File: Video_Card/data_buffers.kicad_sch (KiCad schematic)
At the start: 2 parts, among them U1 74FCT16245

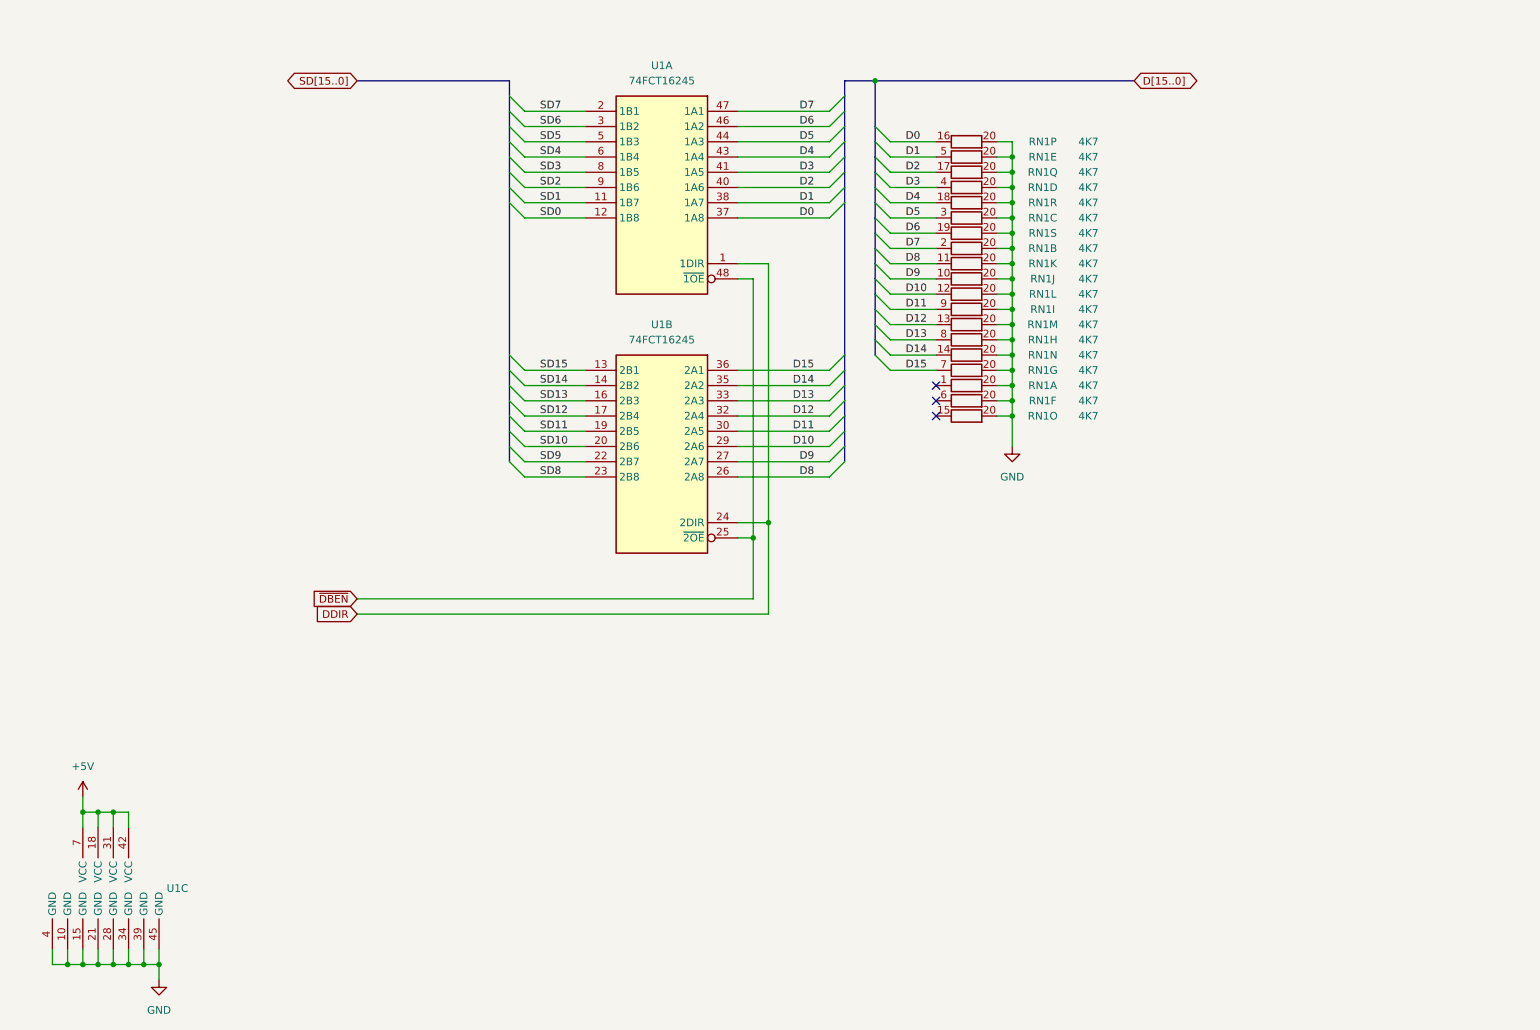
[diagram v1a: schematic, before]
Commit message: Work to date
So much to list ....

* Changed expansion ROM to 16 bit wide to remove some components
* Tried moving peripherals over to an 8 bit dedicated bus, but will have to revert this to reduce component count
* Fleshed out keyboard and I2C controller circuits
* Tried to fit in a font RAM, but I am 50/50 whether this will stick

And a lot more I am sure.
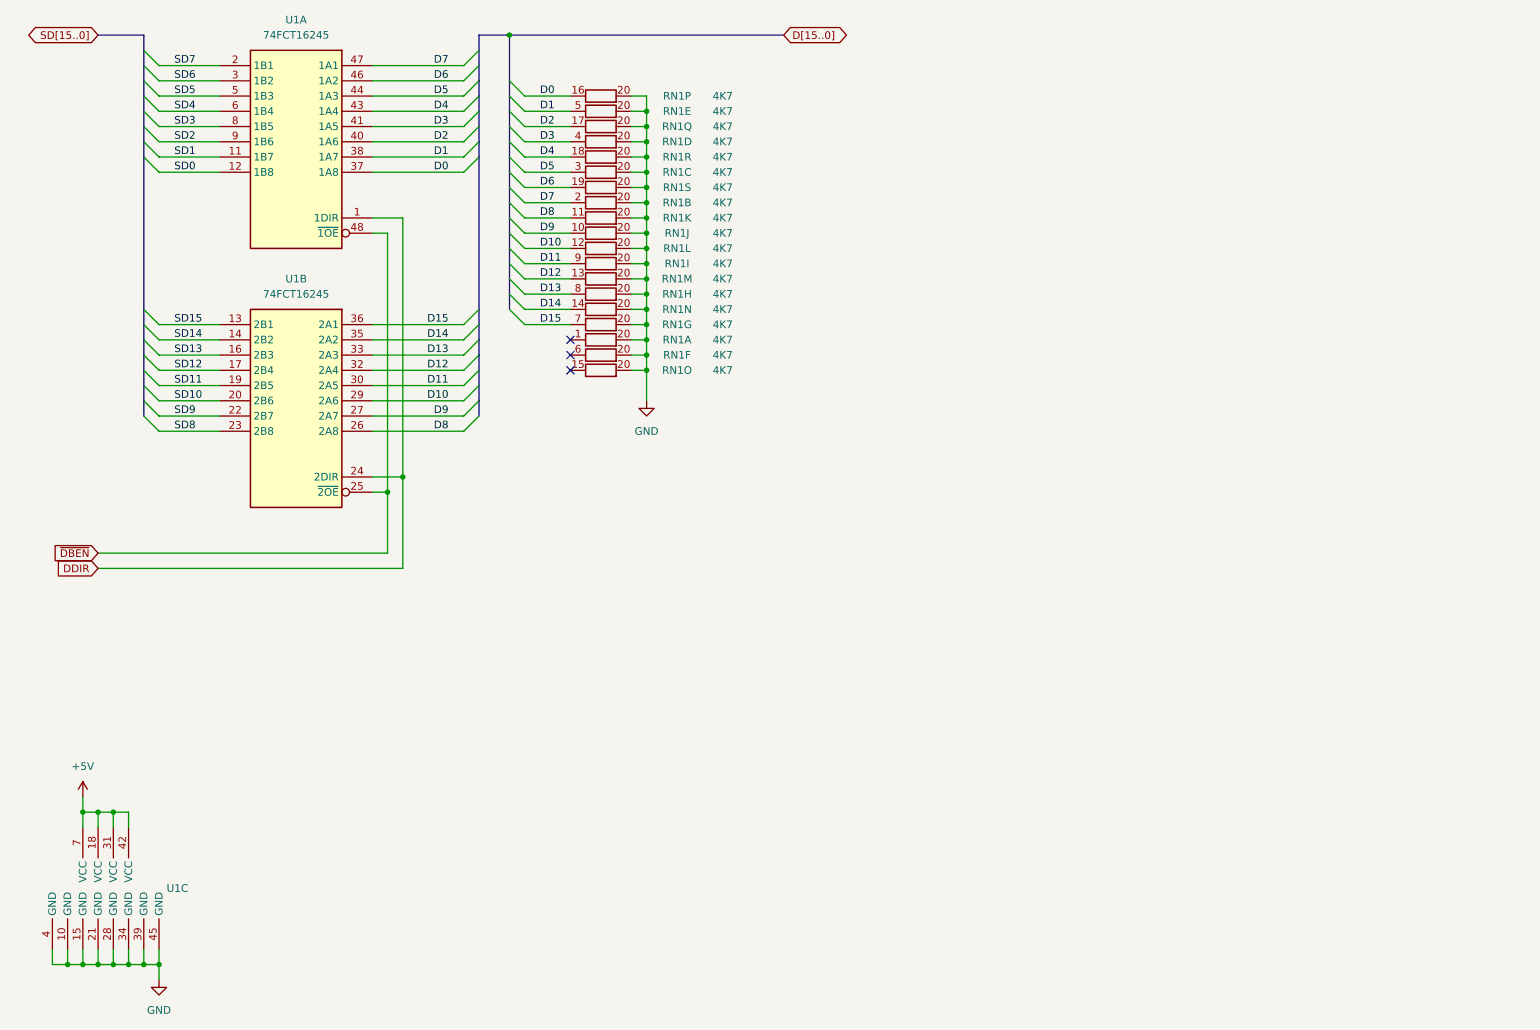
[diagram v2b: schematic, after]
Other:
- moved on the sheet: RN1A, RN1B, RN1C, RN1D, RN1E, RN1F, RN1G, RN1H, RN1I, RN1J, RN1K, RN1L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

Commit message: Final work for rev 1
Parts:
- removed unit 3 of U1
- added U4: SN74AHCT1G32DBV, COMET_footprints:Package_SOT23-5, symbol COMET_symbols:74x1G32
- RN1: value 4K7 -> ~
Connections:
- net D0: now also RN1.15; no longer RN1.16
- net D1: now also RN1.14; no longer RN1.5
- net D10: now also RN1.19; no longer RN1.12
- net D11: now also RN1.3; no longer RN1.9
- net D12: now also RN1.18; no longer RN1.13
- net D13: now also RN1.4; no longer RN1.8
- net D14: now also RN1.17; no longer RN1.14
- net D15: now also RN1.5; no longer RN1.7
- net D2: now also RN1.8; no longer RN1.17
- net D3: now also RN1.13; no longer RN1.4
- net D4: now also RN1.9; no longer RN1.18
- net D5: now also RN1.12; no longer RN1.3
- net D6: now also RN1.10; no longer RN1.19
- net D7: now also RN1.11; no longer RN1.2
- net D8: now also RN1.1; no longer RN1.11
- net D9: now also RN1.2; no longer RN1.10
- net GND: now also U4.1; no longer RN1.20, RN1.20, RN1.20, RN1.20, RN1.20, RN1.20, RN1.20, RN1.20, RN1.20, RN1.20, RN1.20, RN1.20, RN1.20, RN1.20, RN1.20, RN1.20, RN1.20, RN1.20
- new net SYSCLK: U4.4
- new net SYSCLK`: U4.2
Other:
- note added: "U4 SUBSTITUTION: SN74AHCT1G32DBV SN74AHCT1G125DBV"
- moved on the sheet: U1A, U1B

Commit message: Final tweaks before ordering
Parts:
- RN1: value ~ -> 4K7
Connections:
- net D0: now also RN1.5; no longer RN1.15
- net D1: now also RN1.4; no longer RN1.14
- net D10: now also RN1.9; no longer RN1.19
- net D11: now also RN1.13; no longer RN1.3
- net D12: now also RN1.8; no longer RN1.18
- net D13: now also RN1.14; no longer RN1.4
- net D14: now also RN1.7; no longer RN1.17
- net D15: now also RN1.15; no longer RN1.5
- net D2: now also RN1.17; no longer RN1.8
- net D3: now also RN1.3; no longer RN1.13
- net D4: now also RN1.18; no longer RN1.9
- net D5: now also RN1.2; no longer RN1.12
- net D6: now also RN1.19; no longer RN1.10
- net D7: now also RN1.1; no longer RN1.11
- net D8: now also RN1.11; no longer RN1.1
- net D9: now also RN1.12; no longer RN1.2
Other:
- moved on the sheet: RN1A, RN1B, RN1C, RN1D, RN1E, RN1F, RN1G, RN1H, RN1I, RN1J, RN1K, RN1L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
